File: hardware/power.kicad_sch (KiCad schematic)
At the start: 31 parts, among them T2 PA2748NL, U2 LM2596S-3.3, U2 LM2596SX-ADJ, U5 LM2596S-5

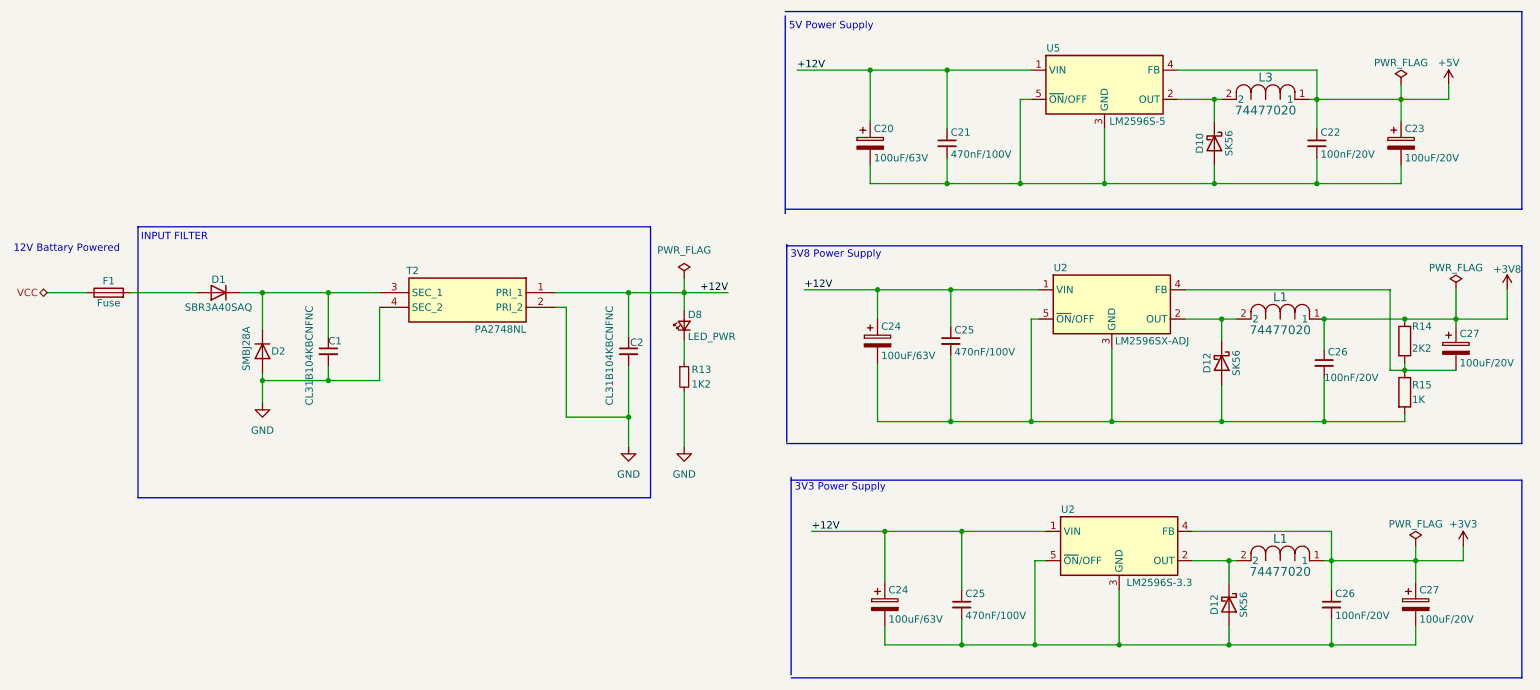
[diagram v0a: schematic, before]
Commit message: * 3V8 Power design fixed * Footprints assigned * Bom exported * PCB filter module placed
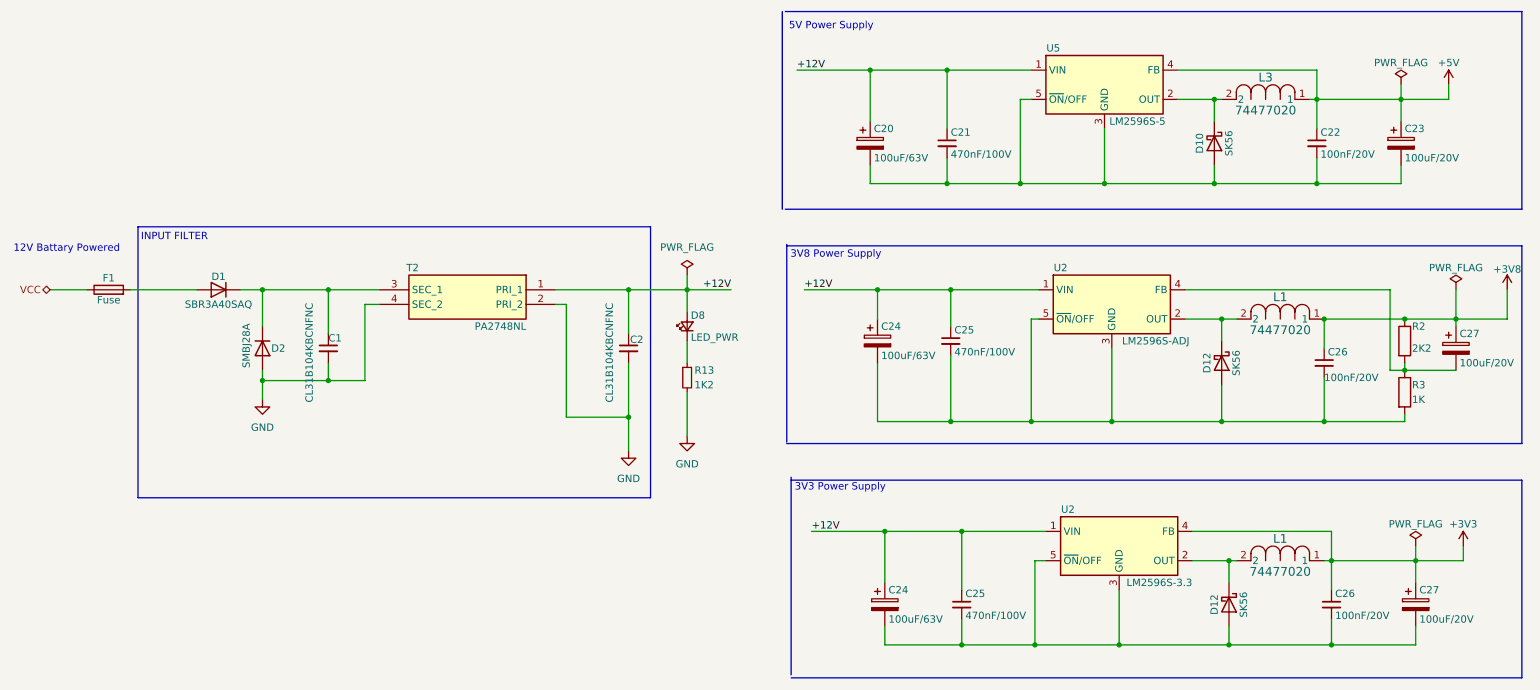
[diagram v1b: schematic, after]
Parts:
- removed U2: LM2596SX-ADJ, Package_TO_SOT_SMD:TO-263-6, symbol Regulator_Switching:LM2596S-3.3
- added U2: LM2596S-ADJ, Package_TO_SOT_SMD:TO-263-5_TabPin3, symbol Regulator_Switching:LM2596S-ADJ
- F1: footprint (none) -> Fuse:Fuse_1206_3216Metric
- L1, L3: footprint Damlama:IND_1280-WE-PD_WRE -> 2023Staj:IND_1280-WE-PD_WRE
- R2: renamed from R14; footprint (none) -> Resistor_SMD:R_0603_1608Metric
- R3: renamed from R15; footprint (none) -> Resistor_SMD:R_0603_1608Metric
- T2: footprint Damlama:PA2748NL -> 2023Staj:PA2748NL
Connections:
- net +12V: now also U2.1 (VIN)
- net at C24.2, C25.2, C26.2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: now also U2.3 (GND), U2.5 (~{ON}/OFF)
- net at D12.1 (K), L1.2: now also U2.2 (OUT)
- net at C27.2, R2.2, R3.1: now also U2.4 (FB)
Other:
- company: (none) -> Hidro Elektronik
- title: (none) -> 2023 Staj Projesi
- moved on the sheet: C1, C2, D1, D2, D8, F1, R13, T2

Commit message: PCB design completed
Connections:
- net GND: now also C20.2, C21.2, C22.2, C23.2, C24.2, C24.2, C25.2, C25.2, C26.2, C26.2, C27.2, D10.2 (A), D12.2 (A), D12.2 (A), R3.2, U2.3 (GND), U2.3 (GND), U2.5 (~{ON}/OFF), U2.5 (~{ON}/OFF), U5.3 (GND), U5.5 (~{ON}/OFF)
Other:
- moved on the sheet: C21, C23, C25, C27
